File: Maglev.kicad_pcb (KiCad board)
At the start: 4 copper layers, 265 x 130 mm, 148 parts, among them IC1 TLV1117LV33DCYR, J1 629722000214, J11 690367190672, J12 690367190672, J2 691103110002, J3 61300621121, J4 61300821121, J6 61300621121, J7 690367191672, J8 690367191672, U1 WE-TVS-82400102, U2 ESP32-C3, U4 TMAG5173A2QDBVRQ1, U5 TPS259474ARPWR, Y1 IQXC-42_830108213209

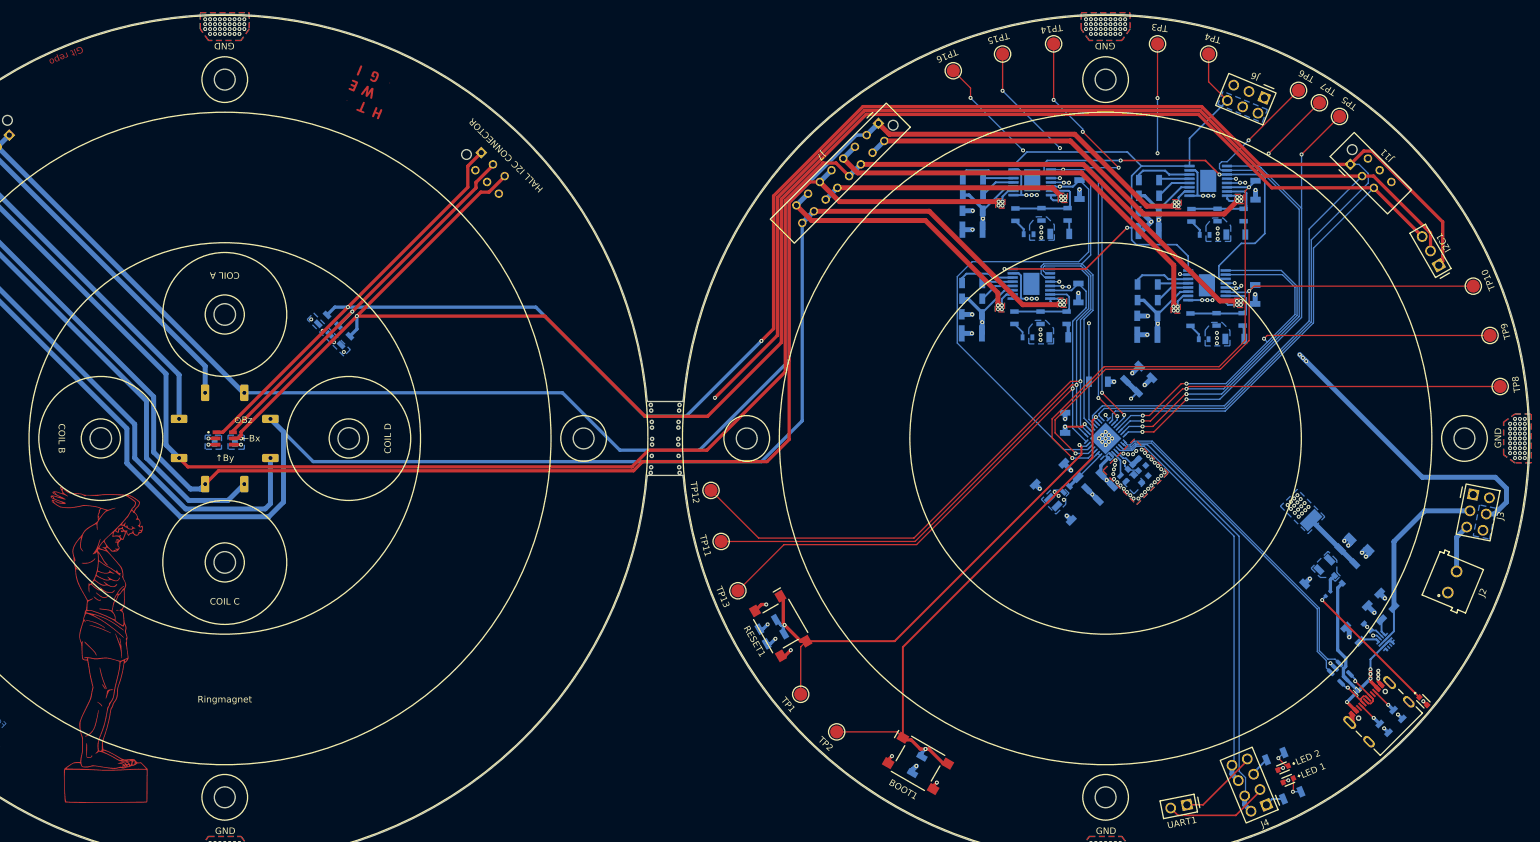
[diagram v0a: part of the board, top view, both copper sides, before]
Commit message: first round adjusting layout tp JLCPCB
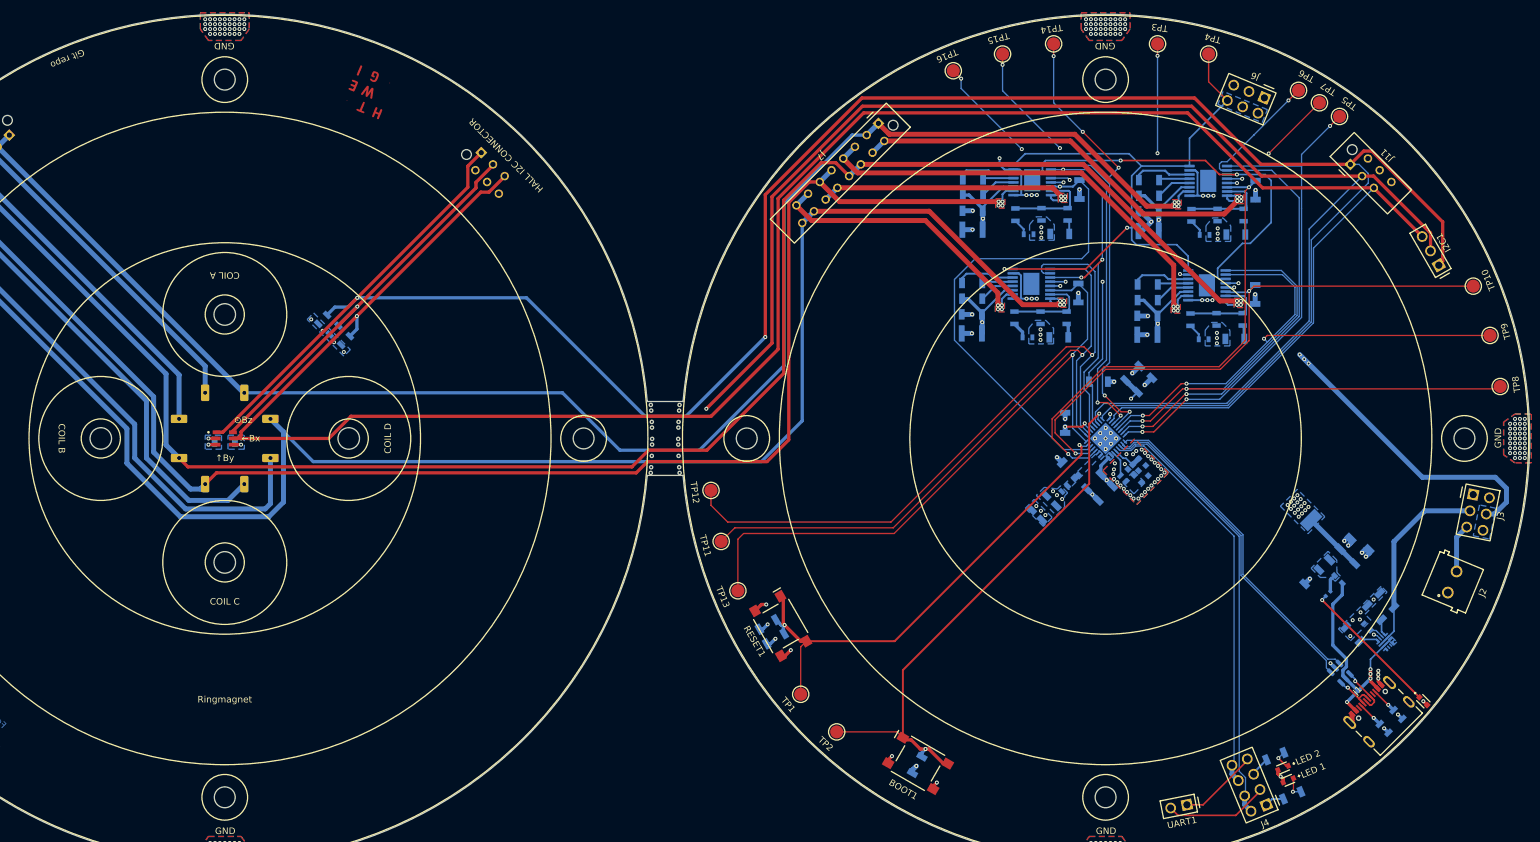
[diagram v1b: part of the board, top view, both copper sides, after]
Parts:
- removed the G*** at (60.8, 131.7)
- moved C3 2.31 mm to (206.3, 111.4), turned to -135 degrees
- moved C7 1.82 mm to (204.8, 109.8), turned to -135 degrees
- moved C9 0.28 mm to (209.4, 104.8)
- moved L5 0.28 mm to (208.7, 107.7)
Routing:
- net /I2C_INT: track 334.4 -> 349.0 mm
- net /VDD3P3: track 12.2 -> 0.00 mm
- net /HBRIDGE_D_ISENSE: track 95.4 -> 102.3 mm
- net GND: track 97.7 -> 91.2 mm, vias 315 -> 312
- net /HBRIDGE_D_DIR: track 104.6 -> 110.5 mm
- net /HBRIDGE_D_PWM: track 96.5 -> 100.6 mm
- net /HBRIDG_ALL_FAULT: track 119.6 -> 122.6 mm
- net /HBRIDGE_ALL_EN: track 114.1 -> 117.0 mm, vias 2 -> 4
- net /HBRIDGE_A_PWM: track 81.9 -> 79.2 mm
- net /HBRIDGE_C_DIR: track 68.3 -> 70.7 mm
- net /I2C_SCL: track 355.2 -> 357.4 mm
- net /I2C_SDA: track 341.6 -> 343.2 mm
- net /BOOT: track 82.8 -> 84.0 mm
- net /HBRIDGE_A_DIR: track 83.5 -> 84.5 mm
- net +V_HB: track 204.0 -> 204.9 mm
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- added copper zone on B.Cu, net /USB Power Circuit/USB_VBUS
- added copper zone on B.Cu, net /VDD3P3

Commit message: made PCB (almost) JLCPCB complient
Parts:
- removed the G*** at (60.8, 131.7)

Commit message: more approvements regarding the manufacturer JLC
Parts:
- moved C3 0.10 mm to (206.4, 111.5)
- moved C7 0.10 mm to (204.7, 109.8)
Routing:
- net /HBRIDGE_B_DIR: track 85.5 -> 78.7 mm
- net /HBRIDGE_B_PWM: track 99.1 -> 93.7 mm
- net /EM_A_P: track 264.0 -> 266.4 mm
- net /I2C_SCL: track 357.4 -> 358.8 mm
- net /I2C_INT: track 349.0 -> 350.1 mm
- net /HBRIDGE_A_PWM: track 79.2 -> 80.1 mm
- net /I2C_SDA: track 343.2 -> 344.0 mm
- net GND: track 91.2 -> 91.5 mm, vias 312 -> 315
- net +3.3V: vias 39 -> 35

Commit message: more approvements regarding the manufacturer JLC
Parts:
- removed MB? (x18): , CUSTOM:BreakLine_1h_D0.5mm_P0.85mm
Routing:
- net /I2C_INT: track 350.1 -> 136.3 mm
- net /I2C_SDA: track 344.0 -> 144.7 mm, vias 2 -> 1
- net /I2C_SCL: track 358.8 -> 159.8 mm, vias 2 -> 1
- net /EM_B_N: track 266.7 -> 122.9 mm
- net /EM_A_P: track 266.4 -> 123.7 mm
- net /EM_B_P: track 273.5 -> 134.5 mm
- net /EM_C_N: track 234.5 -> 99.2 mm
- net /EM_A_N: track 245.8 -> 112.2 mm
- net /EM_C_P: track 244.1 -> 117.5 mm
- net /EM_D_P: track 264.0 -> 146.9 mm
- net /EM_D_N: track 239.6 -> 127.9 mm
- net GND: track 91.5 -> 90.2 mm
- net +3.3V: track 41.0 -> 39.7 mm, vias 35 -> 26
- net /BOOT: track 84.0 -> 84.8 mm
- net /HBRIDGE_A_ISENSE: track 91.8 -> 92.4 mm
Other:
- outline, holes or cut-outs redrawn
